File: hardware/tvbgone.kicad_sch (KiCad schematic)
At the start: 7 parts, among them Q1 BS170, SW1 SW_Push, U1 XIAO-ESP32-S6, U2 TSOP382xx

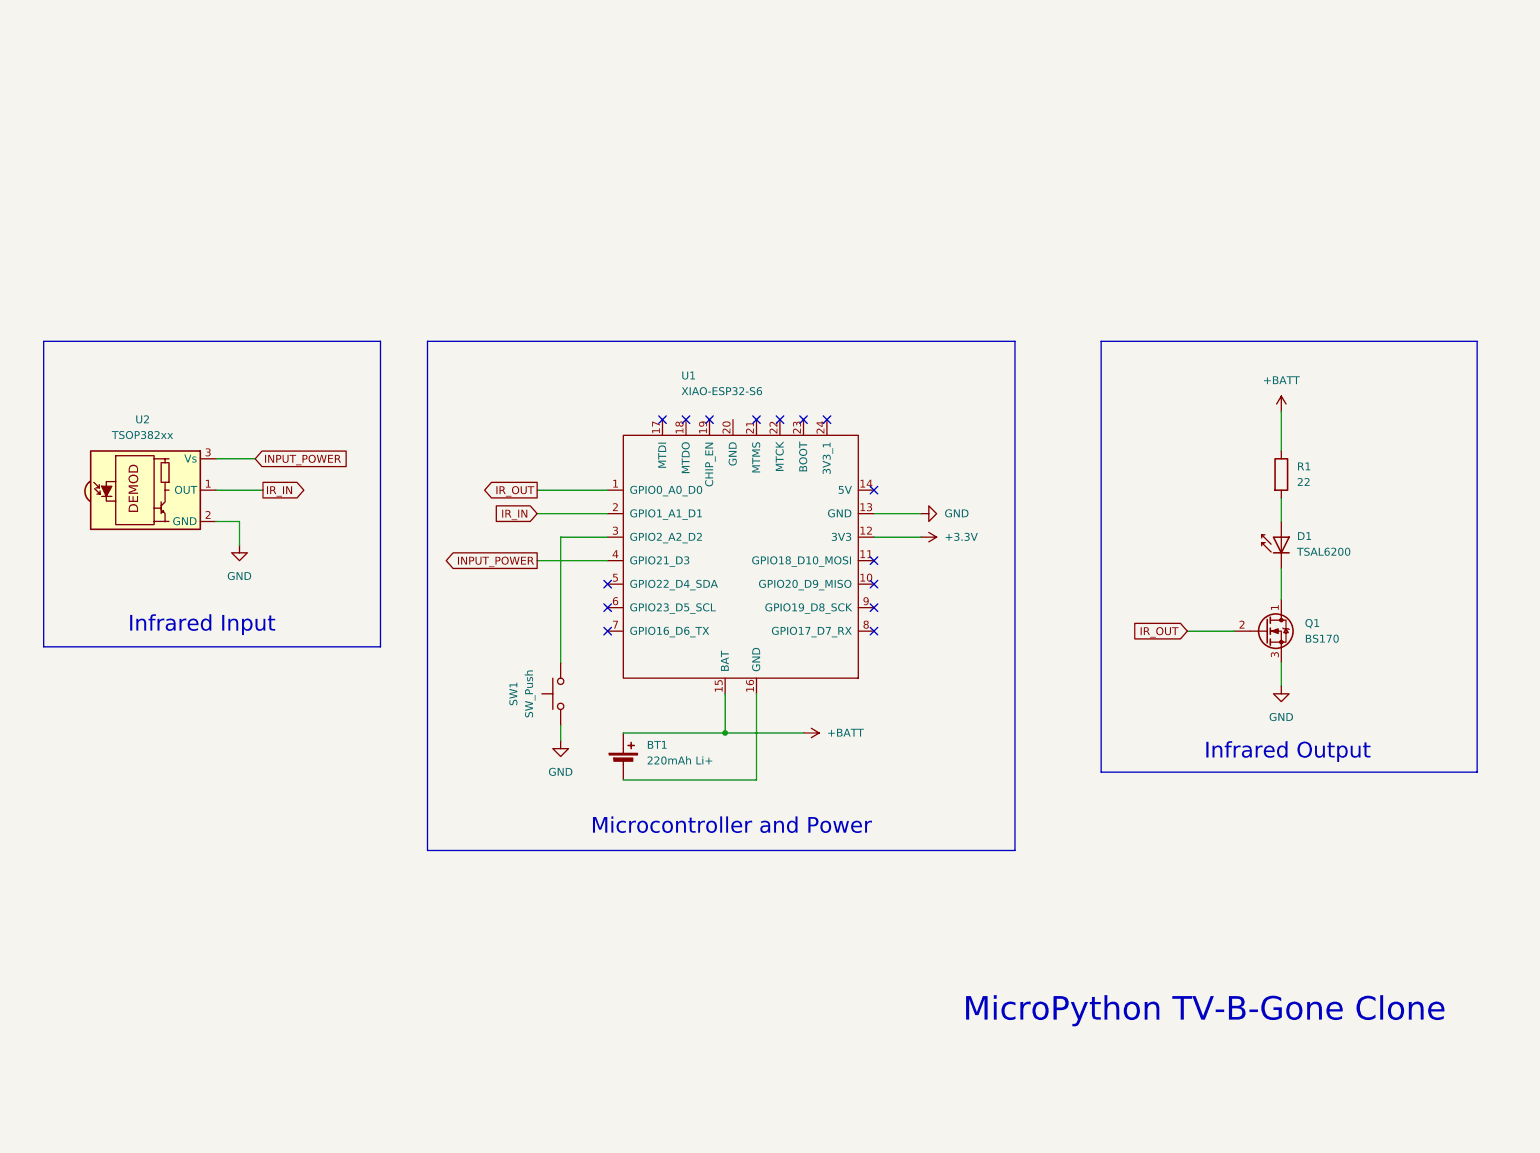
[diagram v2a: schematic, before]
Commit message: Add support for UM TinyS3
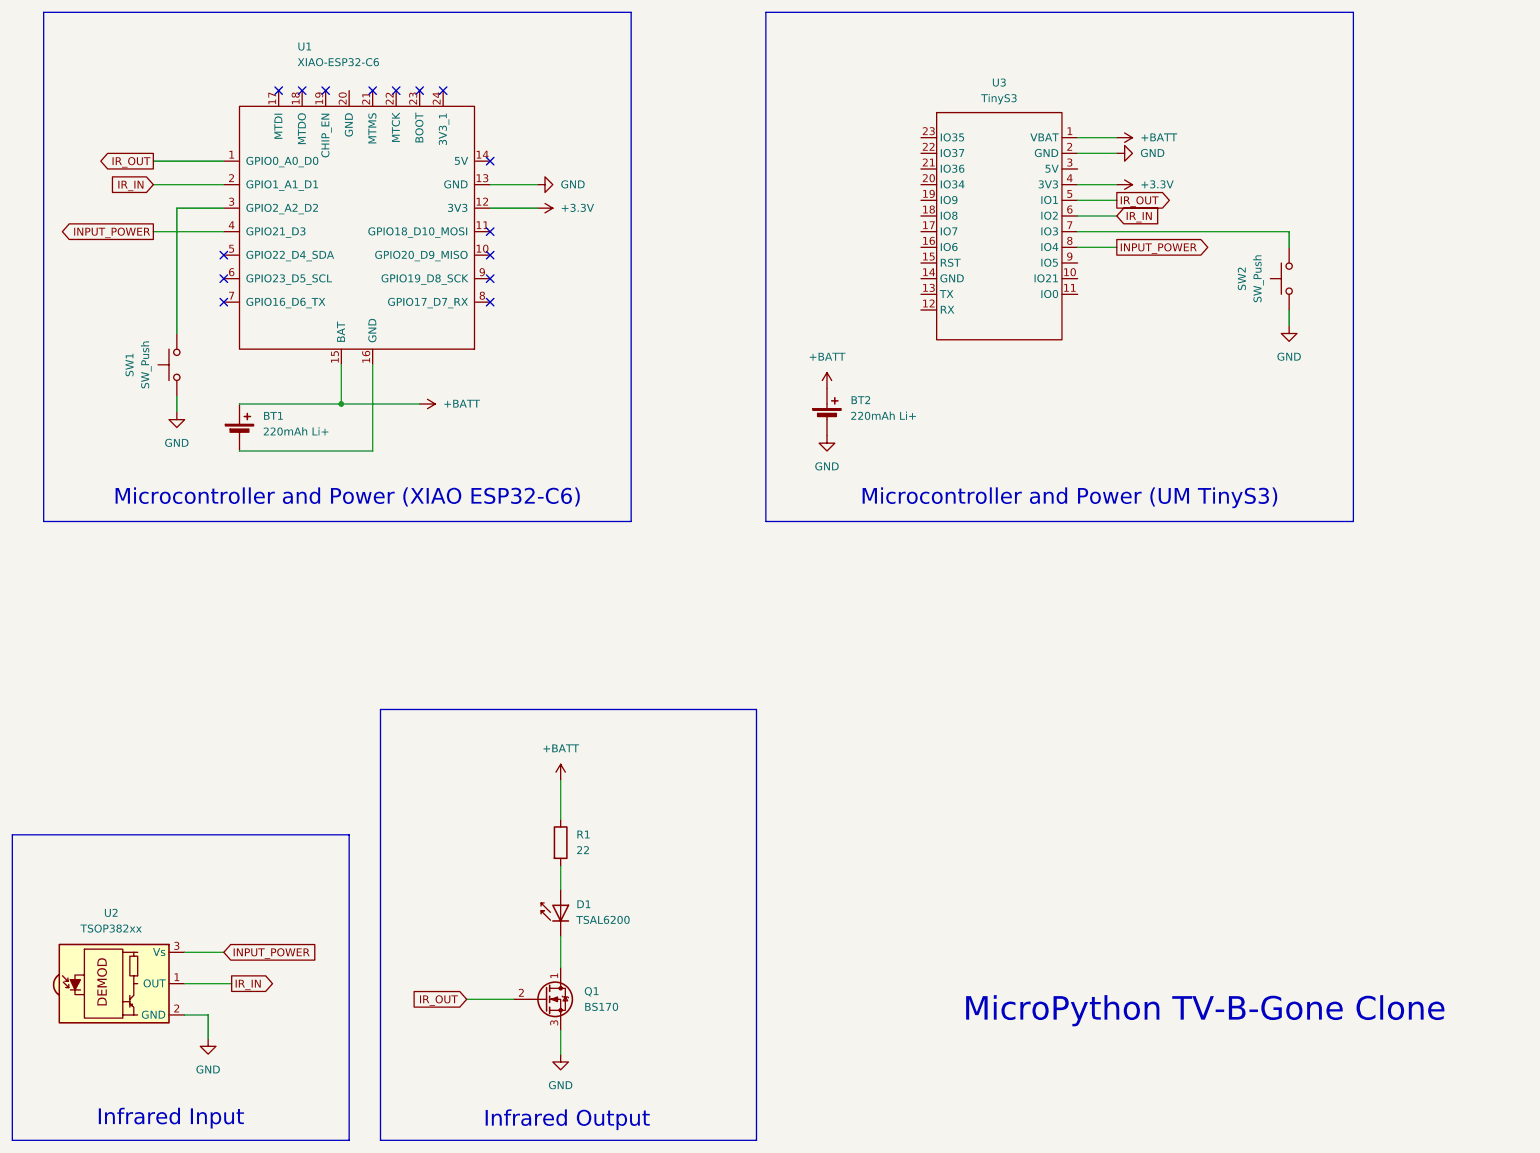
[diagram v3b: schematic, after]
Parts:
- added BT2: 220mAh Li+, symbol Device:Battery_Cell
- added SW2: SW_Push, symbol Switch:SW_Push
- added U3: TinyS3, symbol TinyS3:TinyS3_Symbol
- U1: value XIAO-ESP32-S6 -> XIAO-ESP32-C6
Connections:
- net +3.3V: now also U3.4 (3V3)
- net +BATT: now also BT2.1 (+), U3.1 (VBAT)
- net GND: now also BT2.2 (-), SW2.1, U3.2 (GND)
- net INPUT_POWER: now also U3.8 (IO4)
- net IR_IN: now also U3.6 (IO2)
- net IR_OUT: now also U3.5 (IO1)
- new net: SW2.2, U3.7 (IO3)
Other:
- note added: "Microcontroller and Power (UM TinyS3)"
- note added: "Microcontroller and Power (XIAO ESP32-C6)"
- note removed: "Microcontroller and Power"
- moved on the sheet: BT1, D1, Q1, R1, SW1, U1, U2

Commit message: Add Mitsubishi codes.
Also change transistor to VN3205 and add docs.
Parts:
- removed Q1: BS170, Package_TO_SOT_THT:TO-92_Inline, symbol Transistor_FET:BS170
- added Q1: VN3205, symbol Transistor_FET:Q_NMOS_SGD
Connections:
- net GND: now also Q1.1 (S)
- net IR_OUT: now also Q1.2 (G)
- net at D1.1 (K): now also Q1.3 (D)
